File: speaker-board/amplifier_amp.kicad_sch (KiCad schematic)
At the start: 23 parts, among them J1 Conn_01x02_Pin, U4 LM3886T_NOPB

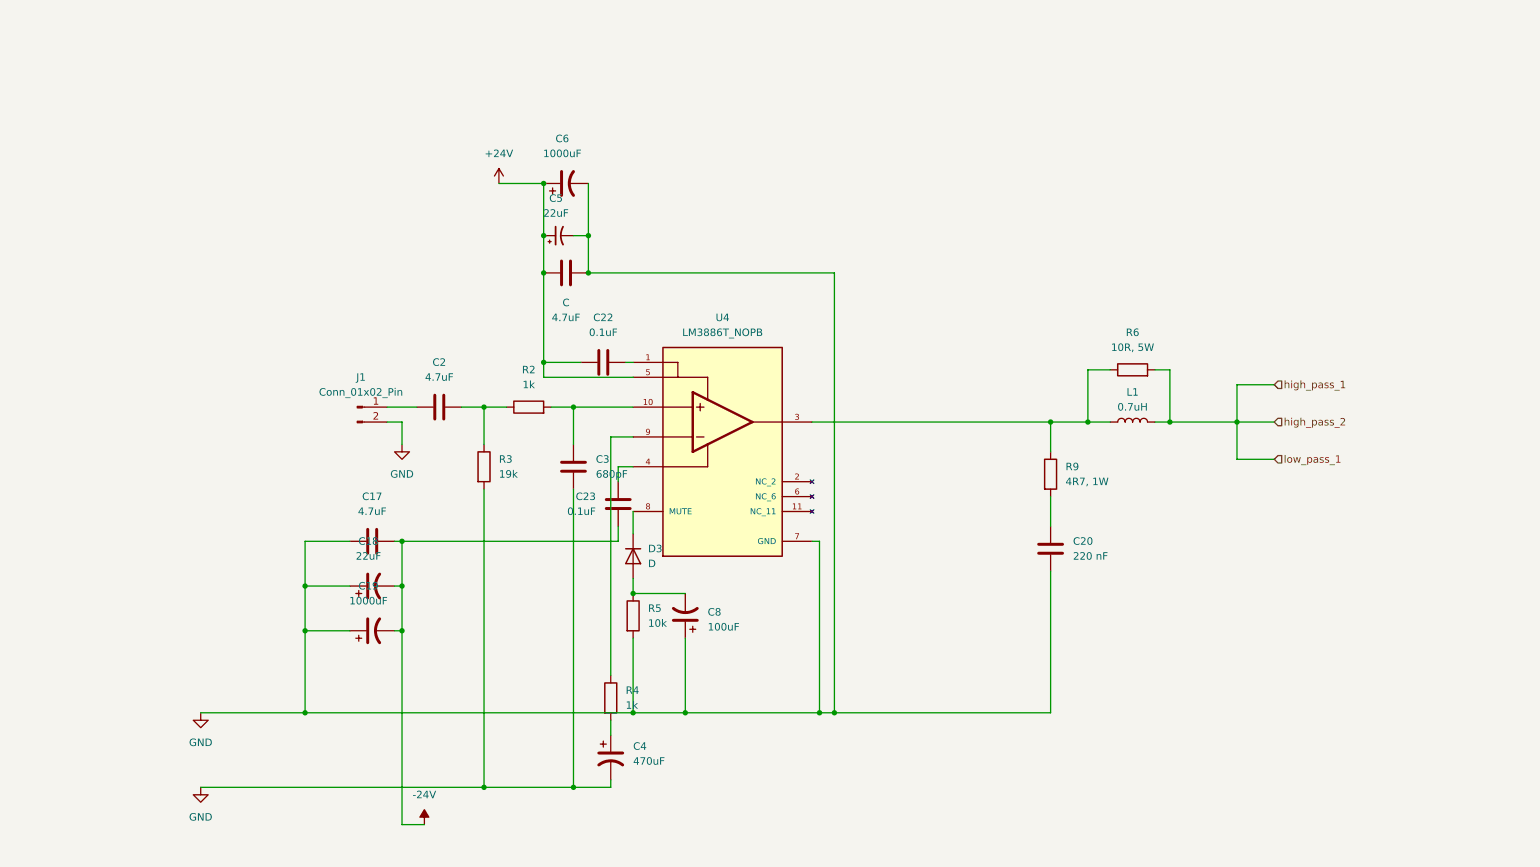
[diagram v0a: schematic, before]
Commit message: Add Amplifier — do half of amp schematic
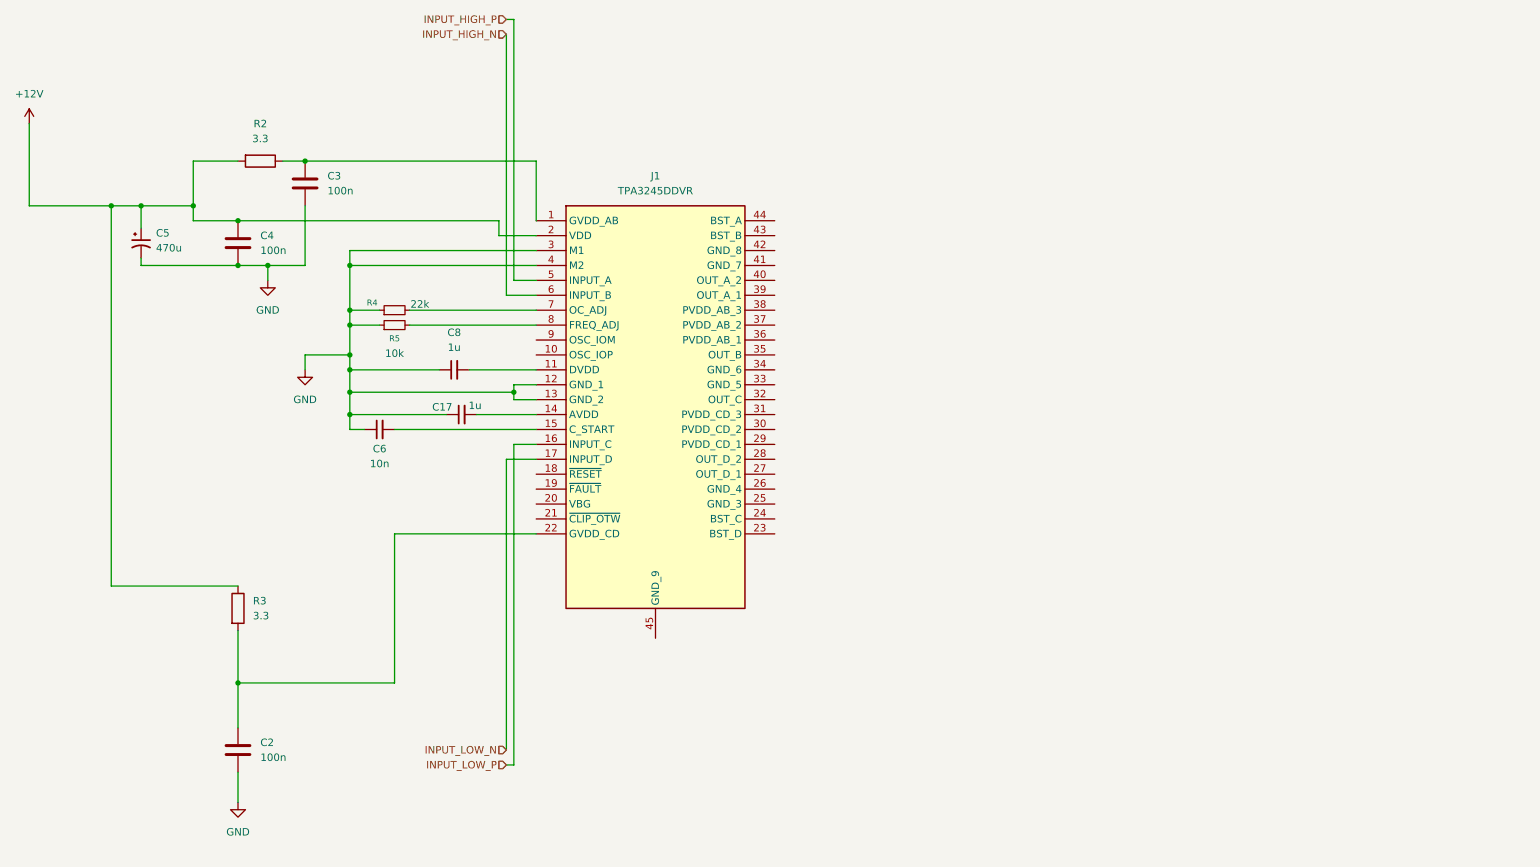
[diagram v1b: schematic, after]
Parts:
- removed 4.7uF: C, symbol Device:C
- removed C17: 4.7uF, symbol Device:C
- removed C18: 22uF, symbol Device:C_Polarized_US
- removed C19, C6: 1000uF, symbol Device:C_Polarized_US
- removed C20: 220 nF, symbol Device:C
- removed C22, C23: 0.1uF, symbol Device:C
- removed C4: 470uF, symbol Device:C_Polarized_US
- removed C8: 100uF, symbol Device:C_Polarized_US
- removed D3: D, symbol Device:D
- removed J1: Conn_01x02_Pin, symbol Connector:Conn_01x02_Pin
- removed L1: 0.7uH, symbol Device:L
- removed R4: 1k, symbol Device:R
- removed R5: 10k, symbol Device:R
- removed R6: 10R, 5W, symbol Device:R
- removed R9: 4R7, 1W, symbol Device:R
- removed U4: LM3886T_NOPB, LM3886T_NOPB:TO170P2027X462X2082-11, symbol LM3886T_NOPB:LM3886T_NOPB
- added C17, C8: 1u, symbol Device:C_Small
- added C4: 100n, symbol Device:C
- added C6: 10n, symbol Device:C_Small
- added J1: TPA3245DDVR, SOP64P810X120-45N, symbol TPA3245DDVR:TPA3245DDVR
- added R4: 22k, symbol Device:R_Small
- added R5: 10k, symbol Device:R_Small
- C2: value 4.7uF -> 100n
- C3: value 680pF -> 100n
- C5: value 22uF -> 470u
- R2: value 1k -> 3.3
- R3: value 19k -> 3.3
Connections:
- net GND: now also C2.2, C17.1, C4.2, C6.1, C8.1, J1.12 (GND_1), J1.13 (GND_2), J1.3 (M1), J1.4 (M2), R4.1, R5.1; no longer R3.2
- net at C3.1: now also R2.1, J1.1 (GVDD_AB); no longer R2.2
- net +24V renamed +12V
- net +12V: now also R2.2, R3.1, C4.1, J1.2 (VDD)
- new net: C2.1, J1.22 (GVDD_CD), R3.2
- new net: C6.2, J1.15 (C_START)
- new net: J1.7 (OC_ADJ), R4.2
- new net: C8.2, J1.11 (DVDD)
- new net: C17.2, J1.14 (AVDD)
- new net: J1.8 (FREQ_ADJ), R5.2
- new net INPUT_HIGH_N: J1.6 (INPUT_B)
- new net INPUT_HIGH_P: J1.5 (INPUT_A)
- new net INPUT_LOW_N: J1.17 (INPUT_D)
- new net INPUT_LOW_P: J1.16 (INPUT_C)
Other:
- company: (none) -> Dhairya Gupta & Charan Pradeep
- title: (none) -> Amplifier Circuit

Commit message: Amplifier subsheet done
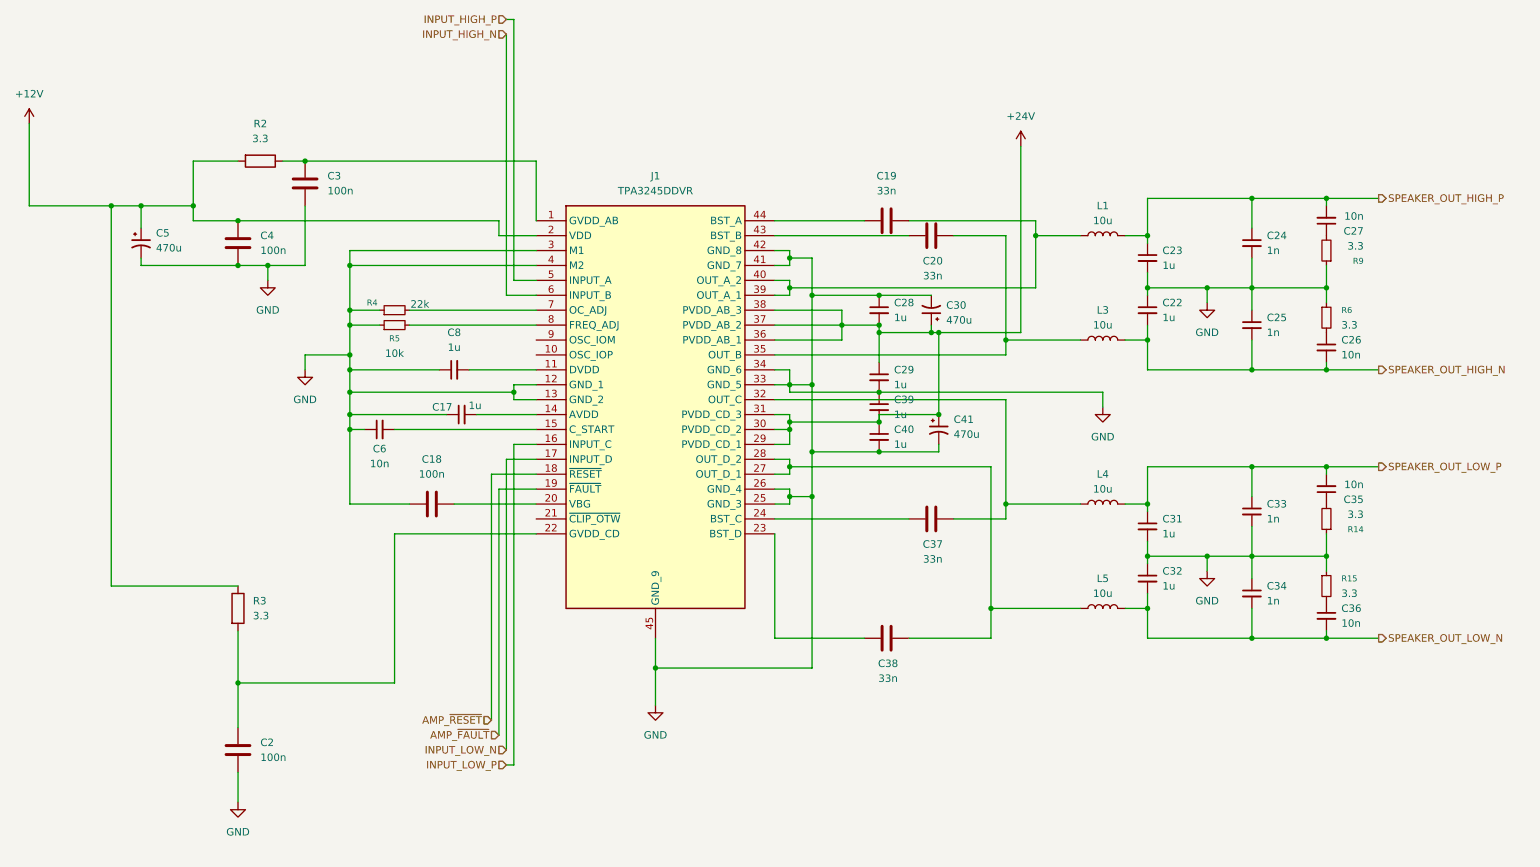
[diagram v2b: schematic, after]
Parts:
- added C18: 100n, symbol Device:C
- added C19, C20, C37, C38: 33n, symbol Device:C
- added C22, C23, C28, C29, C31, C32, C39, C40: 1u, symbol Device:C_Small
- added C24, C25, C33, C34: 1n, symbol Device:C_Small
- added C26, C27, C35, C36: 10n, symbol Device:C_Small
- added C30, C41: 470u, symbol Device:C_Polarized_Small_US
- added L1, L3, L4, L5: 10u, symbol Device:L
- added R14, R15, R6, R9: 3.3, symbol Device:R_Small
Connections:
- net GND: now also J1.25 (GND_3), J1.26 (GND_4), J1.33 (GND_5), J1.34 (GND_6), J1.41 (GND_7), J1.42 (GND_8), J1.45 (GND_9), C18.1, C22.1, C23.2, C24.2, C25.1, C28.1, C29.2, C30.2, C31.2, C32.1, C33.2, C34.1, C39.1, C40.2, C41.2, R14.1, R15.1, R6.1, R9.1
- net AMP_~{RESET}: now reaches J1.18 (~{RESET})
- net AMP_~{FAULT}: now reaches J1.19 (~{FAULT})
- net at J1.20 (VBG): now also C18.2
- net at J1.23 (BST_D): now also C38.1
- net at J1.24 (BST_C): now also C37.1
- net at J1.27 (OUT_D_1): now also J1.28 (OUT_D_2), C38.2, L5.1
- net +24V: now reaches J1.29 (PVDD_CD_1)
- net +24V: now also J1.30 (PVDD_CD_2), J1.31 (PVDD_CD_3), J1.36 (PVDD_AB_1), J1.37 (PVDD_AB_2), J1.38 (PVDD_AB_3), C28.2, C29.1, C30.1, C39.2, C40.1, C41.1
- net at J1.32 (OUT_C): now also C37.2, L4.1
- net at J1.35 (OUT_B): now also C20.2, L3.1
- net at J1.39 (OUT_A_1): now also J1.40 (OUT_A_2), C19.2, L1.1
- net at J1.43 (BST_B): now also C20.1
- net at J1.44 (BST_A): now also C19.1
- new net: C36.1, R15.2
- new net: C27.1, R9.2
- new net: C26.1, R6.2
- new net: C35.1, R14.2
- new net SPEAKER_OUT_HIGH_N: C22.2, C25.2, C26.2, L3.2
- new net SPEAKER_OUT_HIGH_P: C23.1, C24.1, C27.2, L1.2
- new net SPEAKER_OUT_LOW_N: C32.2, C34.2, C36.2, L5.2
- new net SPEAKER_OUT_LOW_P: C31.1, C33.1, C35.2, L4.2

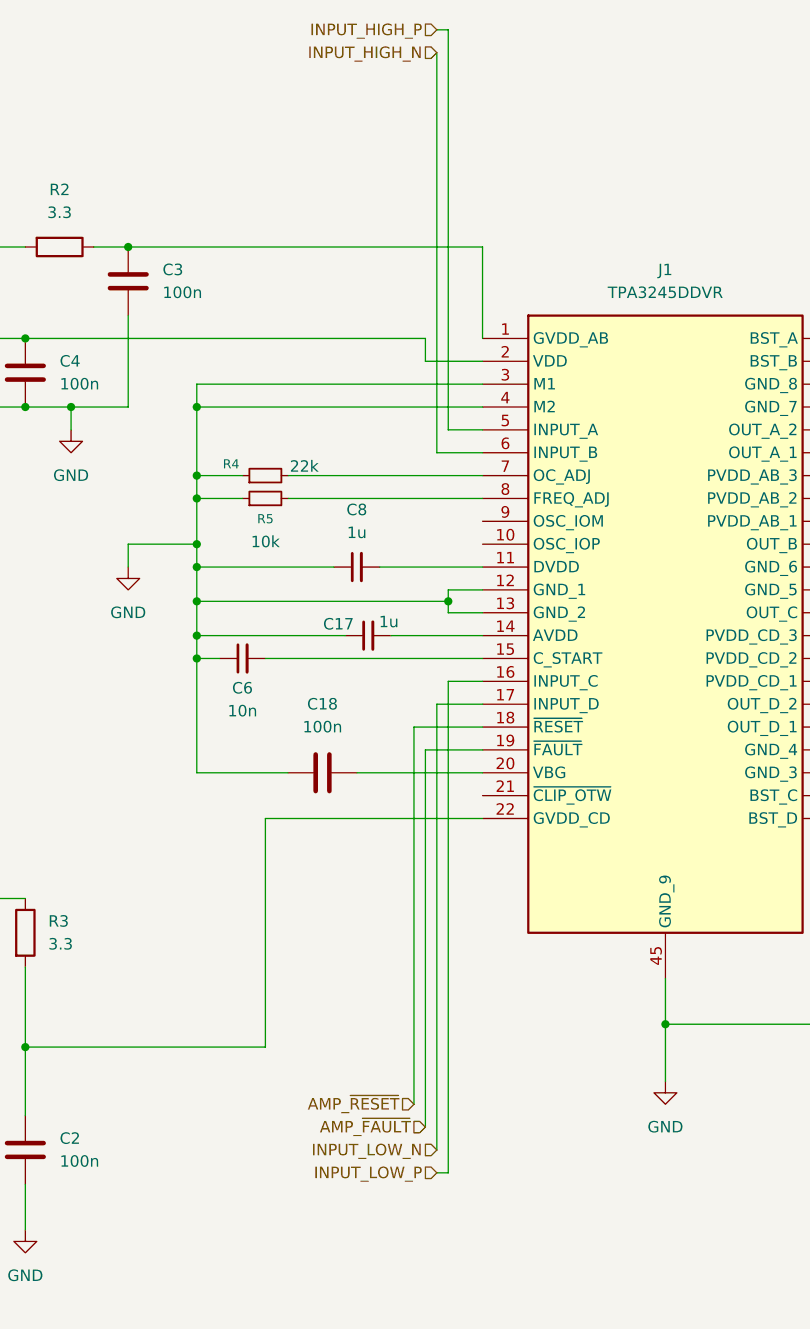
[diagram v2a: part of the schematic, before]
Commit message: fix input coupling
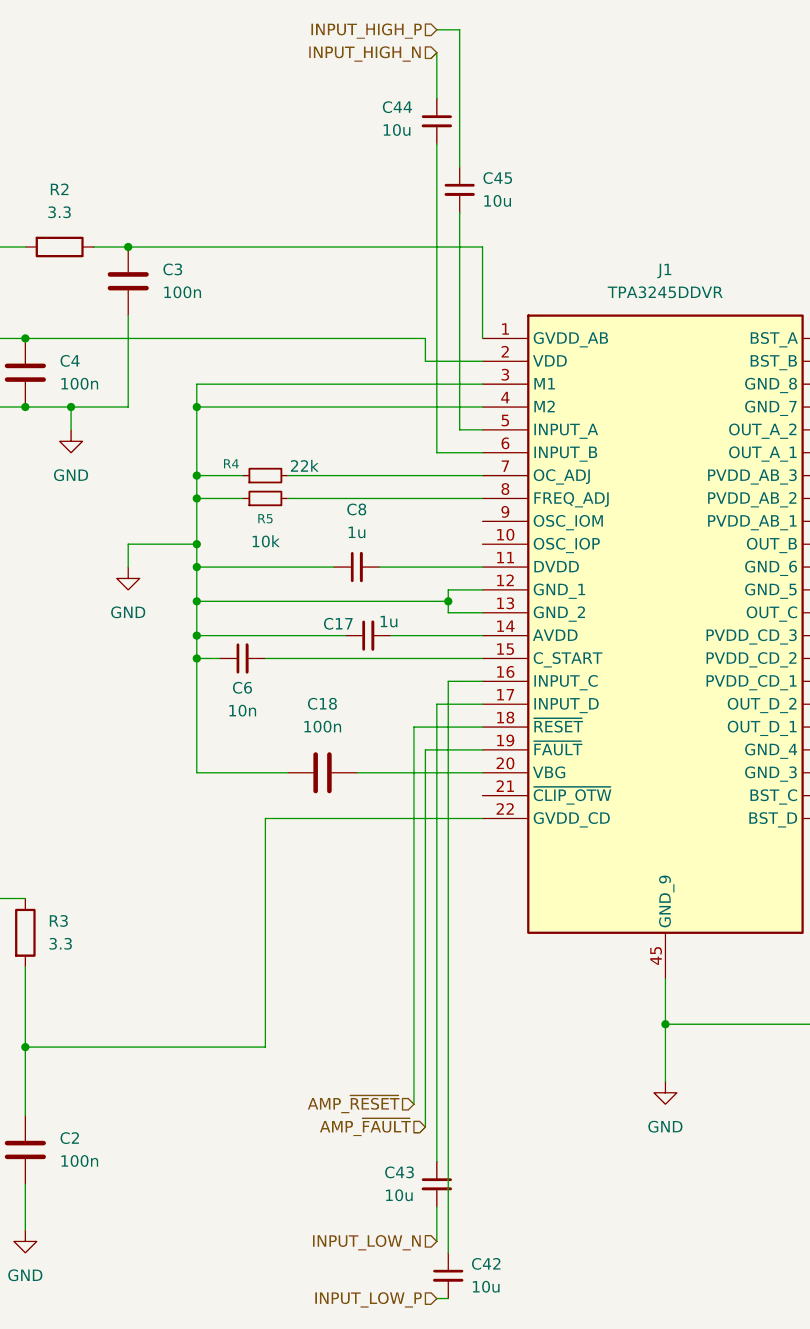
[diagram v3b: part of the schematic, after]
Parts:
- added C42, C43, C44, C45: 10u, symbol Device:C_Small
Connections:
- net INPUT_HIGH_N: now also C44.1; no longer J1.6 (INPUT_B)
- net INPUT_HIGH_P: now also C45.1; no longer J1.5 (INPUT_A)
- net INPUT_LOW_N: now also C43.2; no longer J1.17 (INPUT_D)
- net INPUT_LOW_P: now also C42.2; no longer J1.16 (INPUT_C)
- new net: C44.2, J1.6 (INPUT_B)
- new net: C43.1, J1.17 (INPUT_D)
- new net: C42.1, J1.16 (INPUT_C)
- new net: C45.2, J1.5 (INPUT_A)
